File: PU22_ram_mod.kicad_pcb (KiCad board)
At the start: 2 copper layers, 104.6 x 39.1 mm, 12 parts, among them J1 MOBO, J2 BA8, J3 BA10, J4 GND

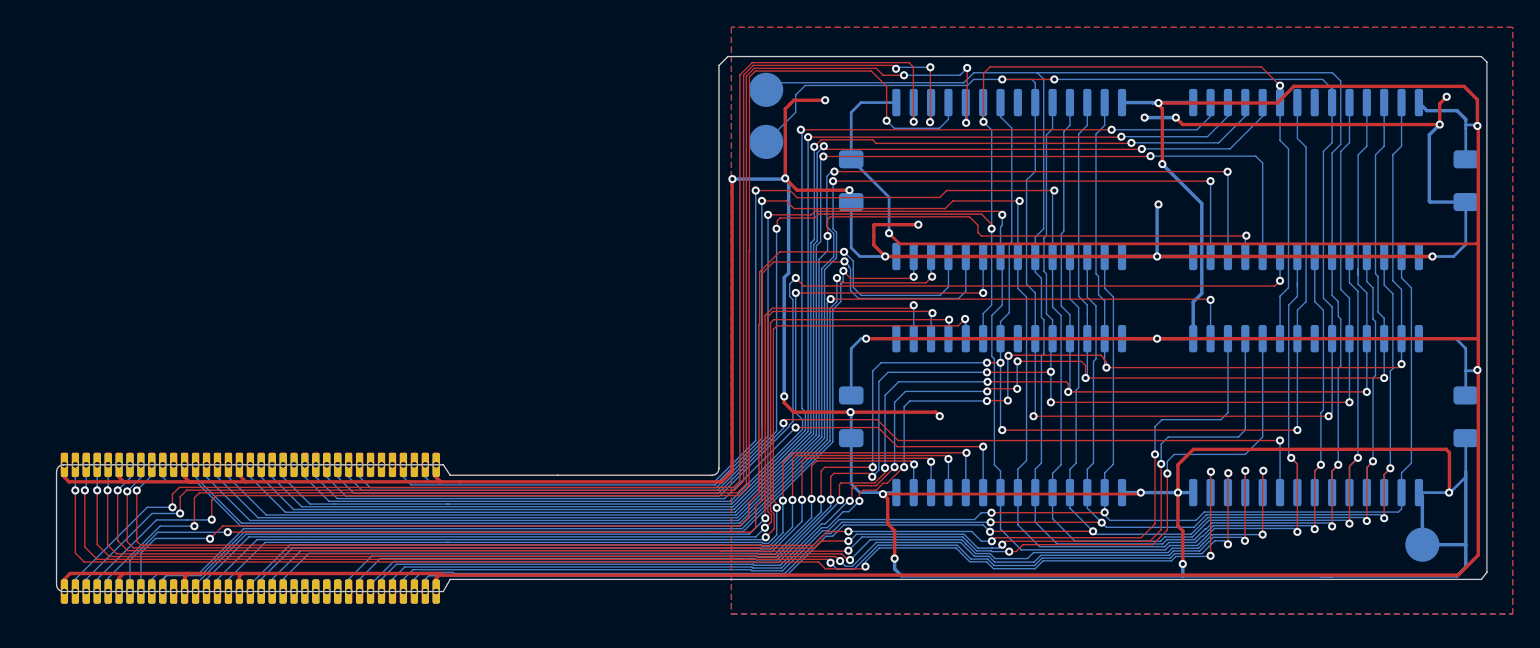
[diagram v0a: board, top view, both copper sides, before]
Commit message: Added silkscreen
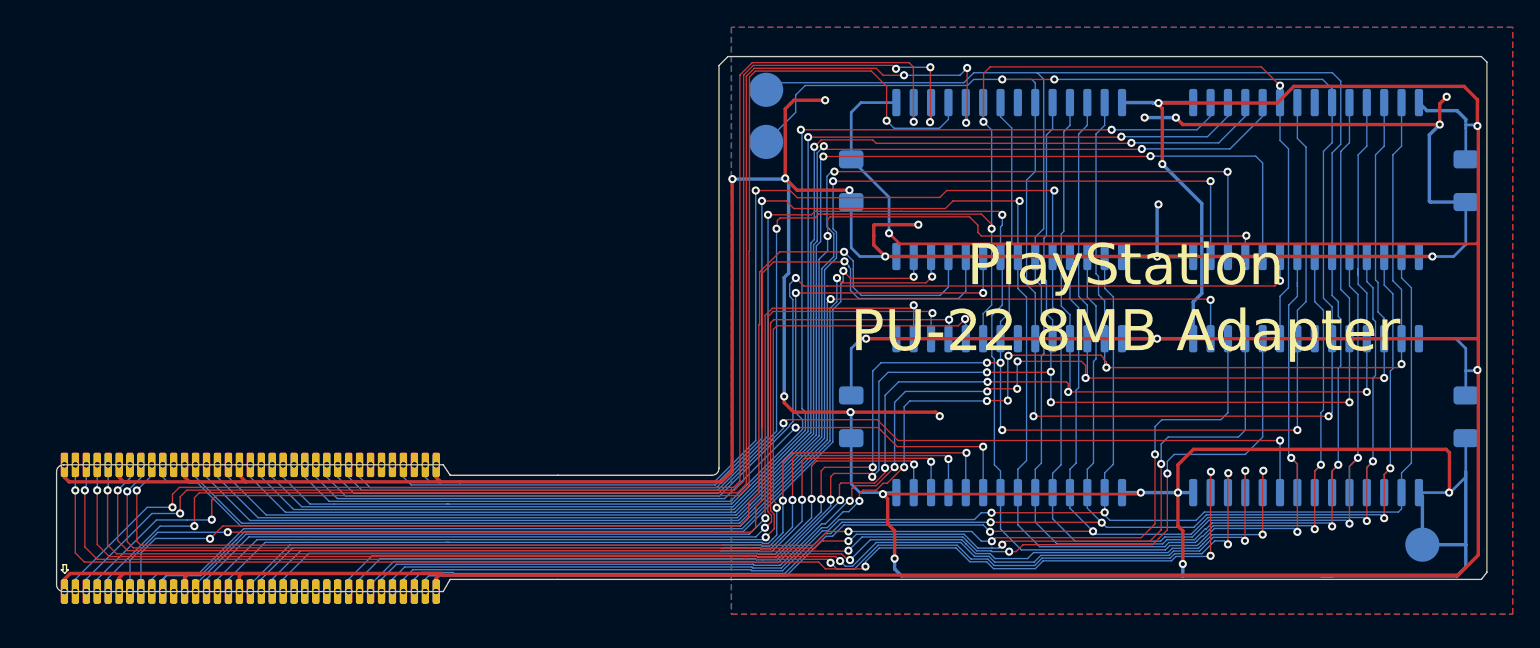
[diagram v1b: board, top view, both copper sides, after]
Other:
- board text added: "PlayStation PU-22 8MB Adapter"

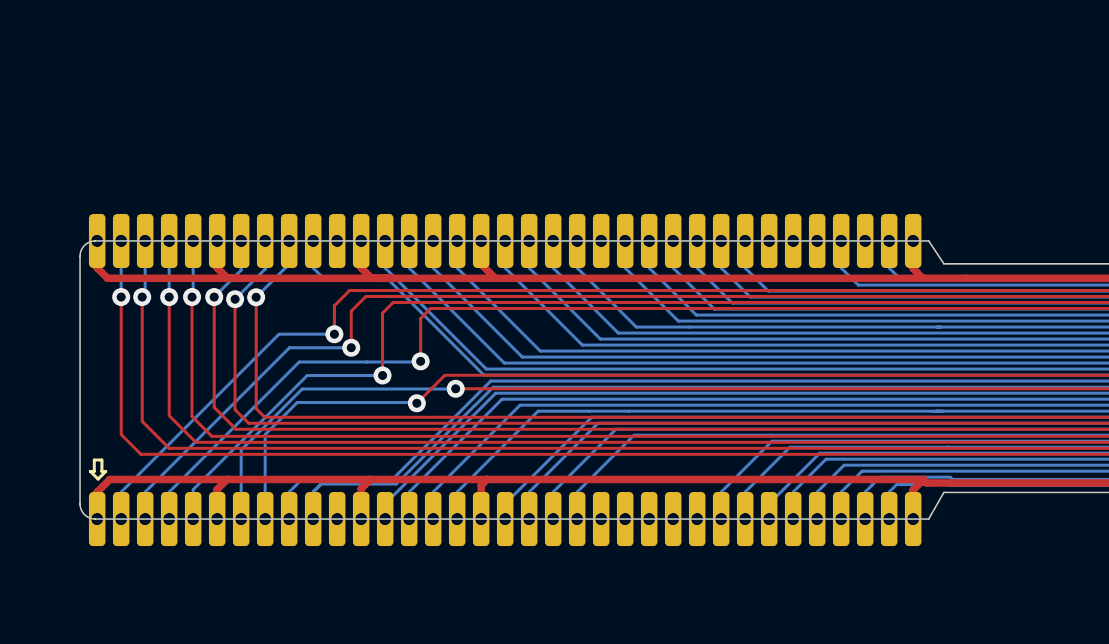
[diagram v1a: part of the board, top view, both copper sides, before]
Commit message: Add some gnd filling in soldered connector too
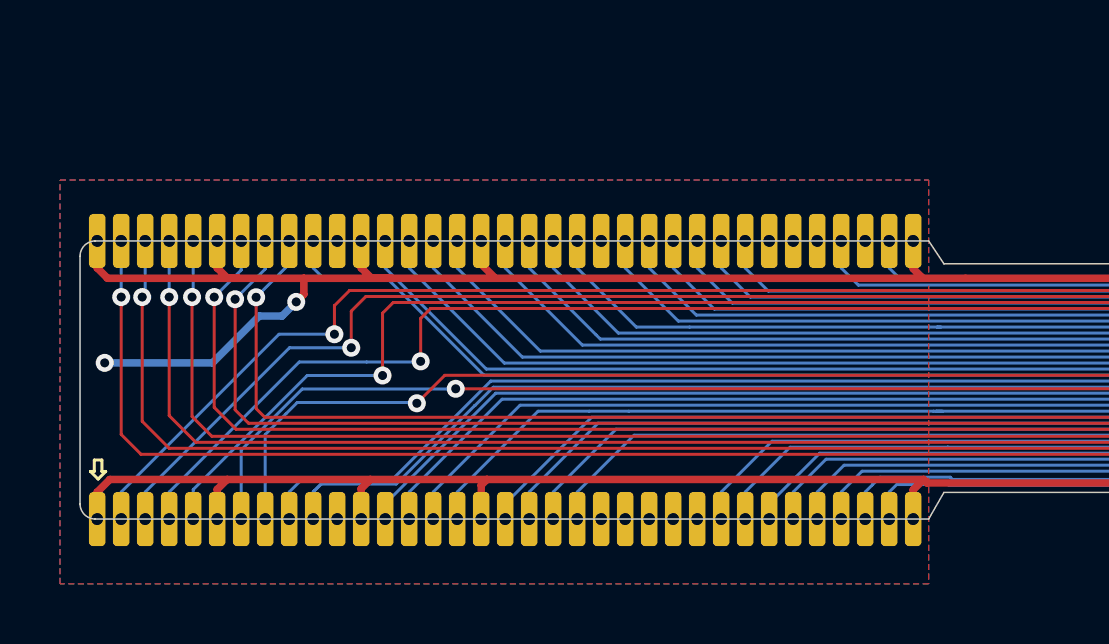
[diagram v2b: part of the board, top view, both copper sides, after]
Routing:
- net GND: track 360.7 -> 368.8 mm, vias 22 -> 24
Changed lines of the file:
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@@
 	(segment
 		(start 77.0712 76.1746)
+		(end 79.248 76.1746)
+		(width 0.25)
+		(layer "F.Cu")
+		(net 2)
+	)
+	(segment
+		(start 79.248 76.1746)
 		(end 85.631 76.1746)
 		(width 0.25)
@@
 	)
 	(segment
+		(start 79.248 76.1746)
+		(end 79.248 76.708)
+		(width 0.25)
+		(layer "F.Cu")
+		(net 2)
+	)
+	(segment
 		(start 121.2088 75.4126)
 		(end 121.2088 54.045579)
@@
 	)
 	(segment
+		(start 79.248 76.708)
+		(end 78.994 76.962)
+		(width 0.25)
+		(layer "F.Cu")
+		(net 2)
+	)
+	(segment
 		(start 125.9586 54.8386)
 		(end 129.794 54.8386)
@@
 	)
 	(via
+		(at 78.994 76.962)
+		(size 0.6)
+		(drill 0.3)
+		(layers "F.Cu" "B.Cu")
+		(net 2)
+	)
+	(via
 		(at 172.4406 59.69)
 		(size 0.6)
@@
 	)
 	(via
+		(at 72.61 78.994)
+		(size 0.6)
+		(drill 0.3)
+		(layers "F.Cu" "B.Cu")
+		(net 2)
+	)
+	(via
 		(at 151.384 49.53)
 		(size 0.6)
@@
 	)
 	(segment
+		(start 77.761852 77.432148)
+		(end 76.2 78.994)
+		(width 0.25)
+		(layer "B.Cu")
+		(net 2)
+	)
+	(segment
 		(start 125.344358 60.904558)
 		(end 125.0188 61.230116)
@@
 	)
 	(segment
+		(start 78.994 76.962)
+		(end 78.523852 77.432148)
+		(width 0.25)
+		(layer "B.Cu")
+		(net 2)
+	)
+	(segment
 		(start 174.879 55.7075)
 		(end 174.879 58.801)
@@
 	)
 	(segment
+		(start 76.2 78.994)
+		(end 72.61 78.994)
+		(width 0.25)
+		(layer "B.Cu")
+		(net 2)
+	)
+	(segment
 		(start 154.178 83.058)
 		(end 133.604 83.058)
@@
 	)
 	(segment
+		(start 78.523852 77.432148)
+		(end 77.761852 77.432148)
+		(width 0.25)
+		(layer "B.Cu")
+		(net 2)
+	)
+	(segment
 		(start 125.0188 61.230116)
 		(end 125.0188 69.9262)
@@
 	)
 	(zone
+		(net 2)
+		(net_name "GND")
+		(layers "F&B.Cu")
+		(hatch edge 0.5)
+		(priority 1)
+		(connect_pads
+			(clearance 0.5)
+		)
+		(min_thickness 0.25)
+		(filled_areas_thickness no)
+		(fill yes
+			(thermal_gap 0.5)
+			(thermal_bridge_width 0.5)
+		)
+		(polygon
+			(pts
+				(xy 71.12 72.898) (xy 100.076 72.898) (xy 100.076 86.36) (xy 71.12 86.36)
+			)
+		)
+	)
+	(zone

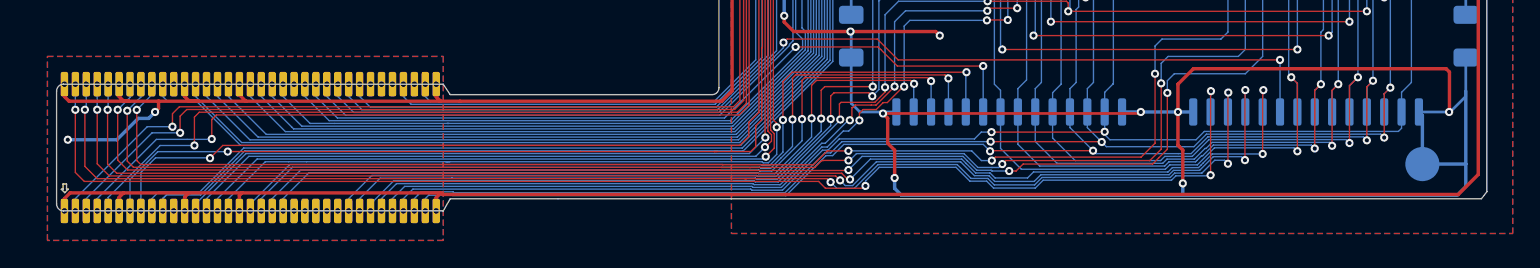
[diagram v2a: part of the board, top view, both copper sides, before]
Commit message: Update silkscreen, begin writing small tutorial
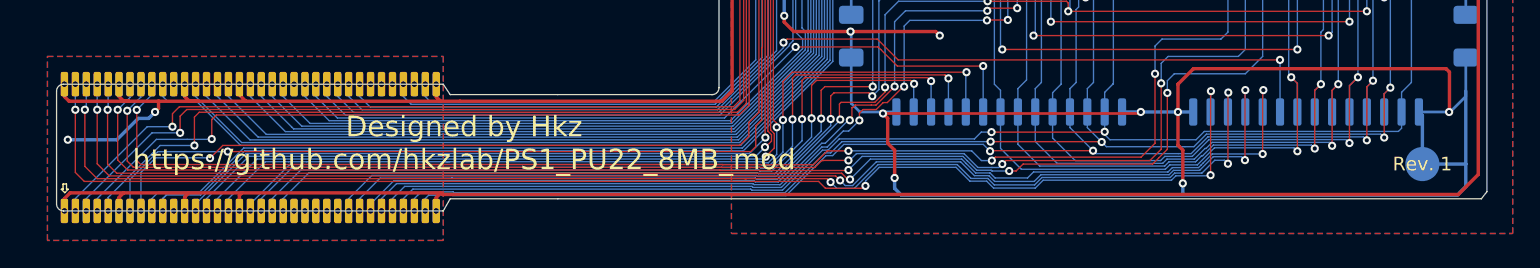
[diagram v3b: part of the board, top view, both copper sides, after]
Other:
- board text added: "Designed by Hkz https://github.com/hkzlab/PS1_PU22_8MB_mod"
- board text added: "Rev. 1"
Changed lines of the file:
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@@
 		(layer "Edge.Cuts")
+	)
+	(gr_text "Rev. 1"
+		(at 171.704 80.772 0)
+		(layer "F.SilkS")
+		(effects
+			(font
+				(size 1 1)
+				(thickness 0.1)
+			)
+		)
+	)
+	(gr_text "Designed by Hkz\nhttps://github.com/hkzlab/PS1_PU22_8MB_mod"
+		(at 101.6 79.248 0)
+		(layer "F.SilkS")
+		(effects
+			(font
+				(size 1.5 1.5)
+				(thickness 0.15)
+			)
+		)
 	)
 	(gr_text "PlayStation\nPU-22 8MB Adapter"
